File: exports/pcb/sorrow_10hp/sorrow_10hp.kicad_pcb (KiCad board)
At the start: 2 copper layers, 50.8 x 128.5 mm, 1 part

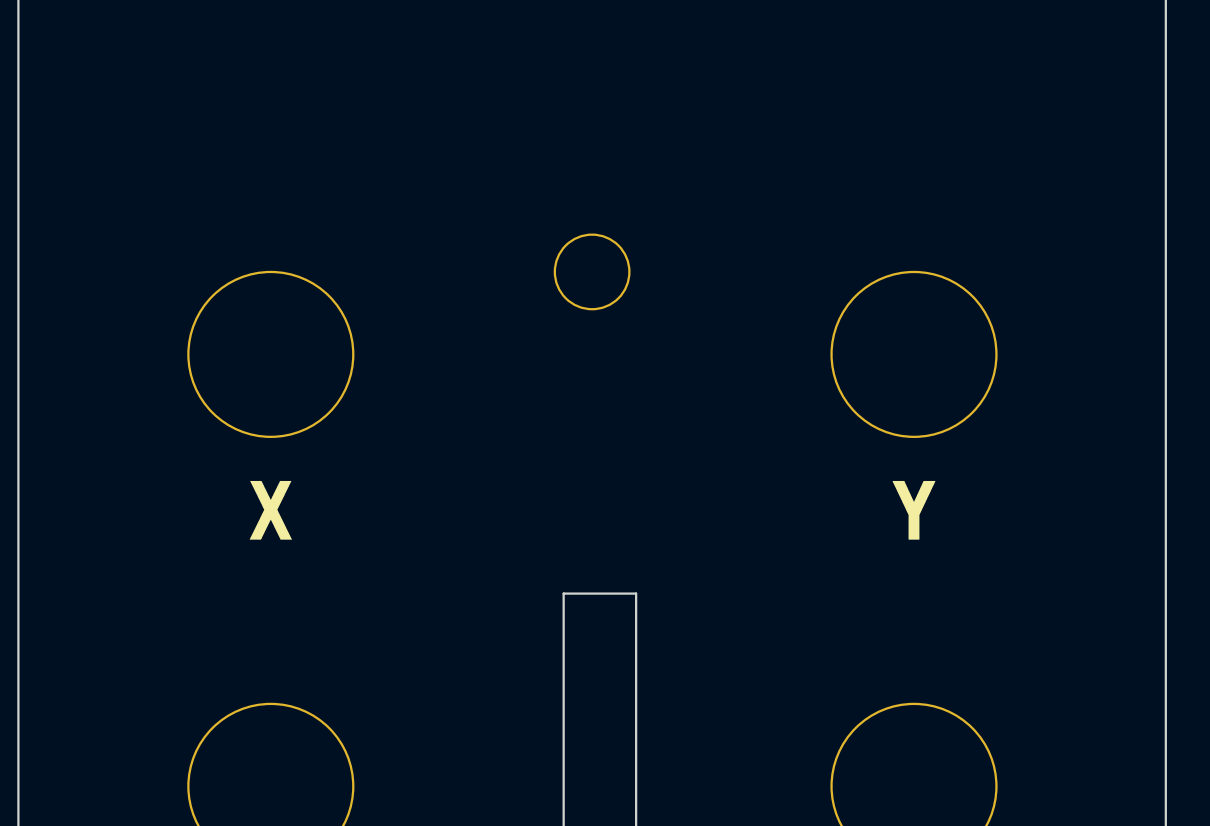
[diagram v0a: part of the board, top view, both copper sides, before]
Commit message: Panels say what the module does, not what the board's pins are called
David's catch, and it applied to both boards.

girl_20hp reproduced the Big Genes' own pin names - P1..P8 on the pots, CV-A..D
on the jacks. That documents the board, not Girl. Relabelled from
eurorack_modules/docs/KSOLOTI_ELEMENTS.md: GEOM / BRIGHT / DAMP / POS on the
resonator row, BOW / BLOW / STRIKE / SPACE on the exciters, CONTOUR and ASSIGN on
the encoders with their push functions under them, PLAY and PAGE on the buttons.

And the thing behind the question: controls whose function changes with a page.
Girl's S4 cycles P5-P7 through level, meta and timbre - three sets, which is what
the dial scales around each pot are there to serve. Sorrow has the same problem
one page smaller: a short press on B7 turns X / Y / DENSITY / CHAOS into the
per-drum density trims plus wildness.

Sorrow's was the worse omission. The word missing from the panel was WILDNESS,
which is the control the module is named around, and there was an empty
HOLE_LABELS_ABOVE tuple sitting there the whole time waiting for it.

The generator grew stacked labels for this: `labels: [...]` prints the primary
name full size and each later page under it, smaller. Jacks carry the board's
name and Girl's use of it, because a Big Genes owner needs to find CV-A and a
Girl player needs to know it is Flow.

Gerbers regenerated for both. NOT ordered - see the preview before spending money.

Co-Authored-By: Claude Opus 5 (1M context) <noreply@anthropic.com>
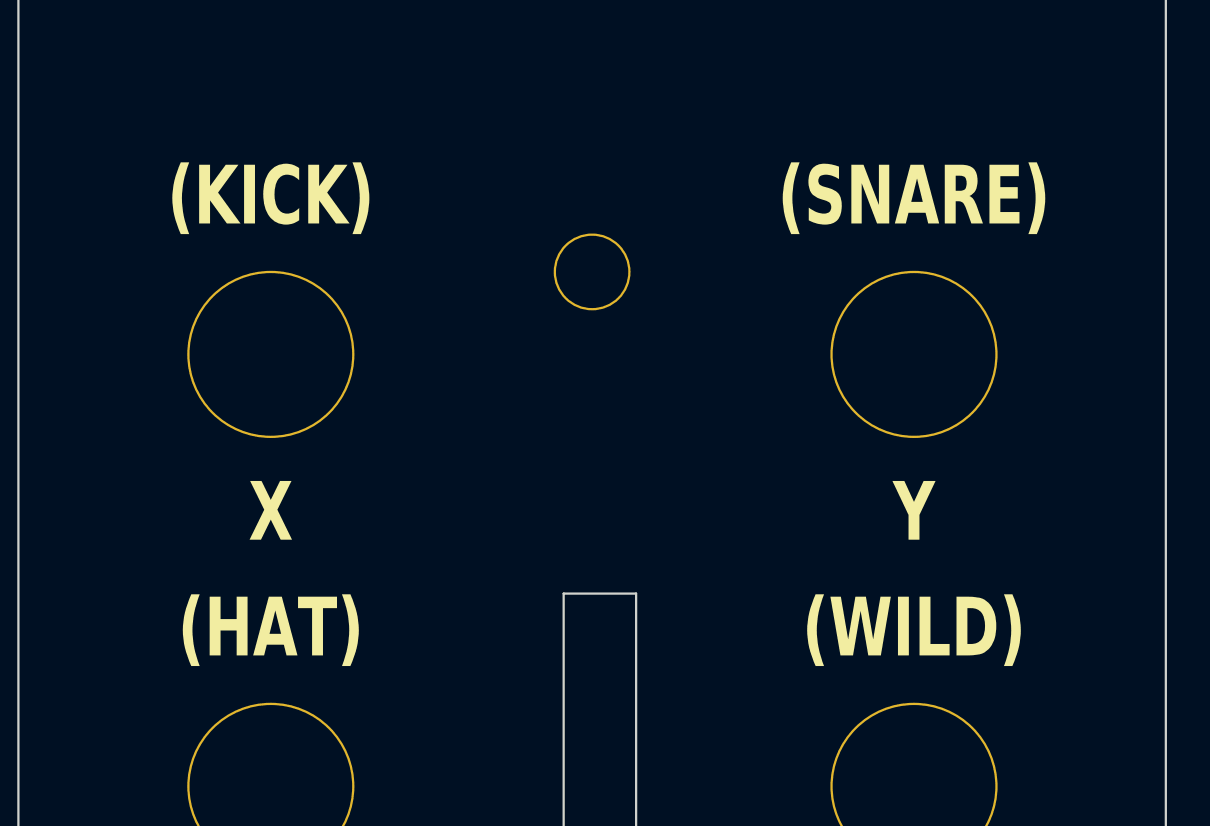
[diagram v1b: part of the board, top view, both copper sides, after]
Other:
- board text added: "(HAT)"
- board text added: "(KICK)"
- board text added: "(SNARE)"
- board text added: "(WILD)"
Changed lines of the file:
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@@
+		(effects (font (size 2.6 1.872) (thickness 0.442) bold))
+	)
+	(gr_text "(WILD)" (at 39.649996 35.027311) (layer "F.SilkS")
 		(effects (font (size 2.6 1.872) (thickness 0.442) bold))
 	)
@@
 		(effects (font (size 2.6 1.872) (thickness 0.442) bold))
 	)
+	(gr_text "(HAT)" (at 11.1755 35.027311) (layer "F.SilkS")
+		(effects (font (size 2.6 1.872) (thickness 0.442) bold))
+	)
 	(gr_text "Y" (at 39.649996 29.904289) (layer "F.SilkS")
+		(effects (font (size 2.6 1.872) (thickness 0.442) bold))
+	)
+	(gr_text "(SNARE)" (at 39.649996 15.904289) (layer "F.SilkS")
 		(effects (font (size 2.6 1.872) (thickness 0.442) bold))
 	)
@@
 		(effects (font (size 2.6 1.872) (thickness 0.442) bold))
 	)
+	(gr_text "(KICK)" (at 11.1755 15.904289) (layer "F.SilkS")
+		(effects (font (size 2.6 1.872) (thickness 0.442) bold))
+	)

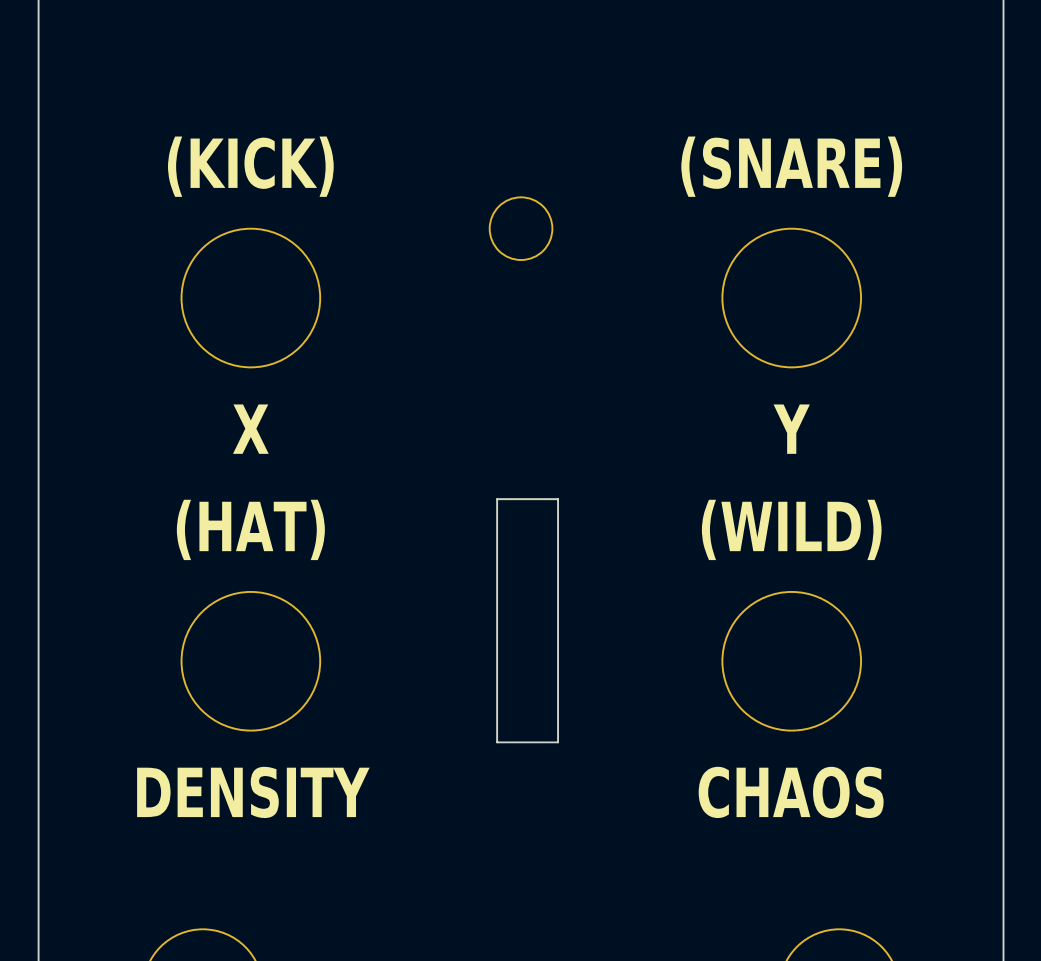
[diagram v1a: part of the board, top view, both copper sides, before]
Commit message: Panels: David's pass on both
Sorrow
  The Home name now sits ABOVE the pot and the Kit name below it, one size
  smaller: DENS-KC, DENS-SN, DENS-HT, WILD. Brackets gone - the size difference
  does that job without punctuation.

  The generator grew LABELS_SECONDARY for it: a tuple of label texts that render
  at 78% of the label size, so a panel can carry a control's second function
  without it reading as a second control.

Girl
  Dial rings gone. CAL label gone - the HOLE stays, because a trimmer behind the
  panel is unreachable without it, and it is easy to put the word back.

  Resonator row is GEOM / BRGT / DAMP / POSN, one name each. P1's model variants
  (DISP, CHRD) come off the panel; the OLED already shows which model is live.

  Jacks: fixed functions say what they do - GEOM, BRGT, DAMP, POSN, V/OCT, FM,
  GATE. Assignable ones keep their board names, CV-A/B/C, because their function
  is whatever E2 last set it to. Everything Girl does not use loses its label:
  MIDI, GTE-1/2, CV-1/2, IN-L/R, HOST.

Both now use the same 2.6 mm labels and 3.0 mm branding as joy_10hp, which they
did not before - Girl was carrying per-control sizes between 1.4 and 2.0. Taking
the dial rings off freed the room for it.

Co-Authored-By: Claude Opus 5 (1M context) <noreply@anthropic.com>
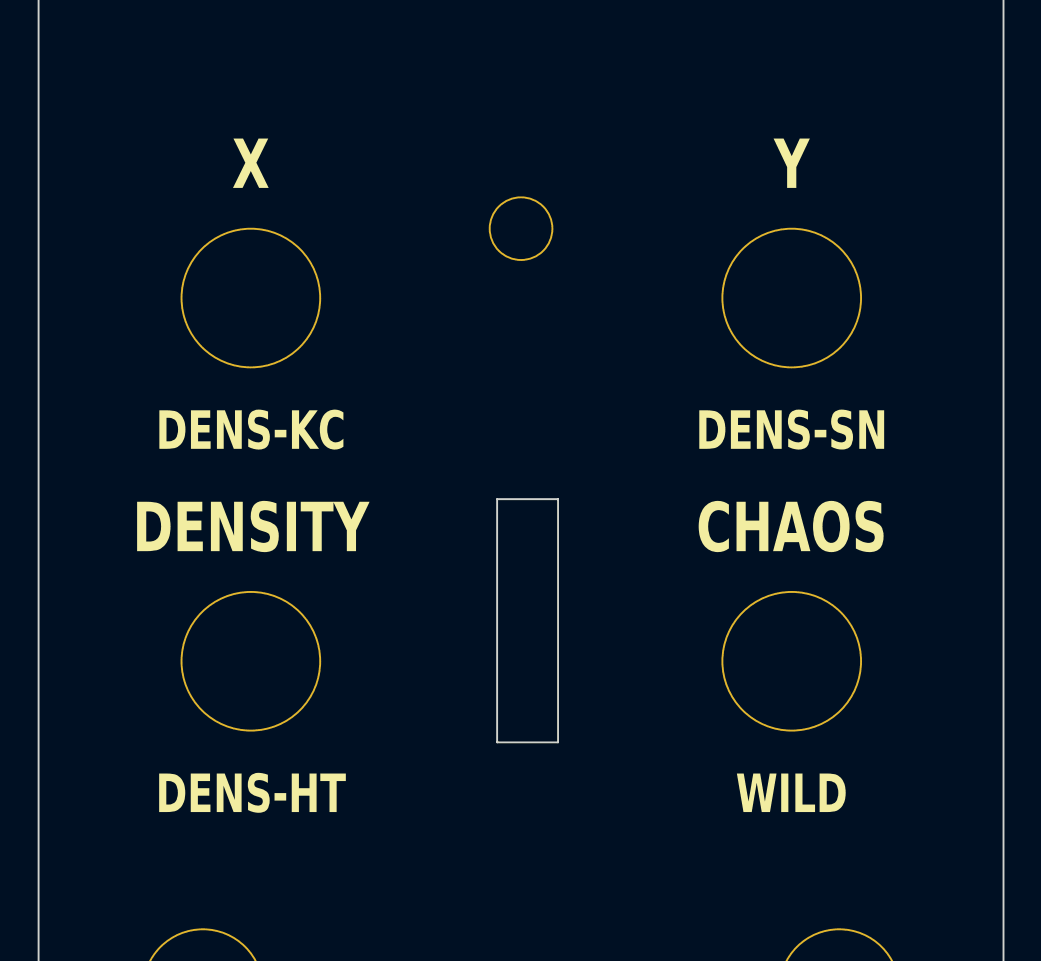
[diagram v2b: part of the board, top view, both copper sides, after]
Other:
- board text added: "DENS-HT"
- board text added: "DENS-KC"
- board text added: "DENS-SN"
- board text added: "WILD"
- board text removed: "(HAT)"
- board text removed: "(KICK)"
- board text removed: "(SNARE)"
- board text removed: "(WILD)"
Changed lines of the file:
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@@
 		(effects (font (size 2.6 1.872) (thickness 0.442) bold))
 	)
-	(gr_text "CHAOS" (at 39.649996 49.027311) (layer "F.SilkS")
+	(gr_text "WILD" (at 39.649996 49.027311) (layer "F.SilkS")
+		(effects (font (size 2.028 1.4602) (thickness 0.345) bold))
+	)
+	(gr_text "CHAOS" (at 39.649996 35.027311) (layer "F.SilkS")
 		(effects (font (size 2.6 1.872) (thickness 0.442) bold))
 	)
-	(gr_text "(WILD)" (at 39.649996 35.027311) (layer "F.SilkS")
+	(gr_text "DENS-HT" (at 11.1755 49.027311) (layer "F.SilkS")
+		(effects (font (size 2.028 1.4602) (thickness 0.345) bold))
+	)
+	(gr_text "DENSITY" (at 11.1755 35.027311) (layer "F.SilkS")
 		(effects (font (size 2.6 1.872) (thickness 0.442) bold))
 	)
-	(gr_text "DENSITY" (at 11.1755 49.027311) (layer "F.SilkS")
+	(gr_text "DENS-SN" (at 39.649996 29.904289) (layer "F.SilkS")
+		(effects (font (size 2.028 1.4602) (thickness 0.345) bold))
+	)
+	(gr_text "Y" (at 39.649996 15.904289) (layer "F.SilkS")
 		(effects (font (size 2.6 1.872) (thickness 0.442) bold))
 	)
-	(gr_text "(HAT)" (at 11.1755 35.027311) (layer "F.SilkS")
+	(gr_text "DENS-KC" (at 11.1755 29.904289) (layer "F.SilkS")
+		(effects (font (size 2.028 1.4602) (thickness 0.345) bold))
+	)
+	(gr_text "X" (at 11.1755 15.904289) (layer "F.SilkS")
 		(effects (font (size 2.6 1.872) (thickness 0.442) bold))
 	)
-	(gr_text "Y" (at 39.649996 29.904289) (layer "F.SilkS")
-		(effects (font (size 2.6 1.872) (thickness 0.442) bold))
-	)
-	(gr_text "(SNARE)" (at 39.649996 15.904289) (layer "F.SilkS")
-		(effects (font (size 2.6 1.872) (thickness 0.442) bold))
-	)
-	(gr_text "X" (at 11.1755 29.904289) (layer "F.SilkS")
-		(effects (font (size 2.6 1.872) (thickness 0.442) bold))
-	)
-	(gr_text "(KICK)" (at 11.1755 15.904289) (layer "F.SilkS")
-		(effects (font (size 2.6 1.872) (thickness 0.442) bold))
-	)
